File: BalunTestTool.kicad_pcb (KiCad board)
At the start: 2 copper layers, 37.2 x 37.1 mm, 17 parts

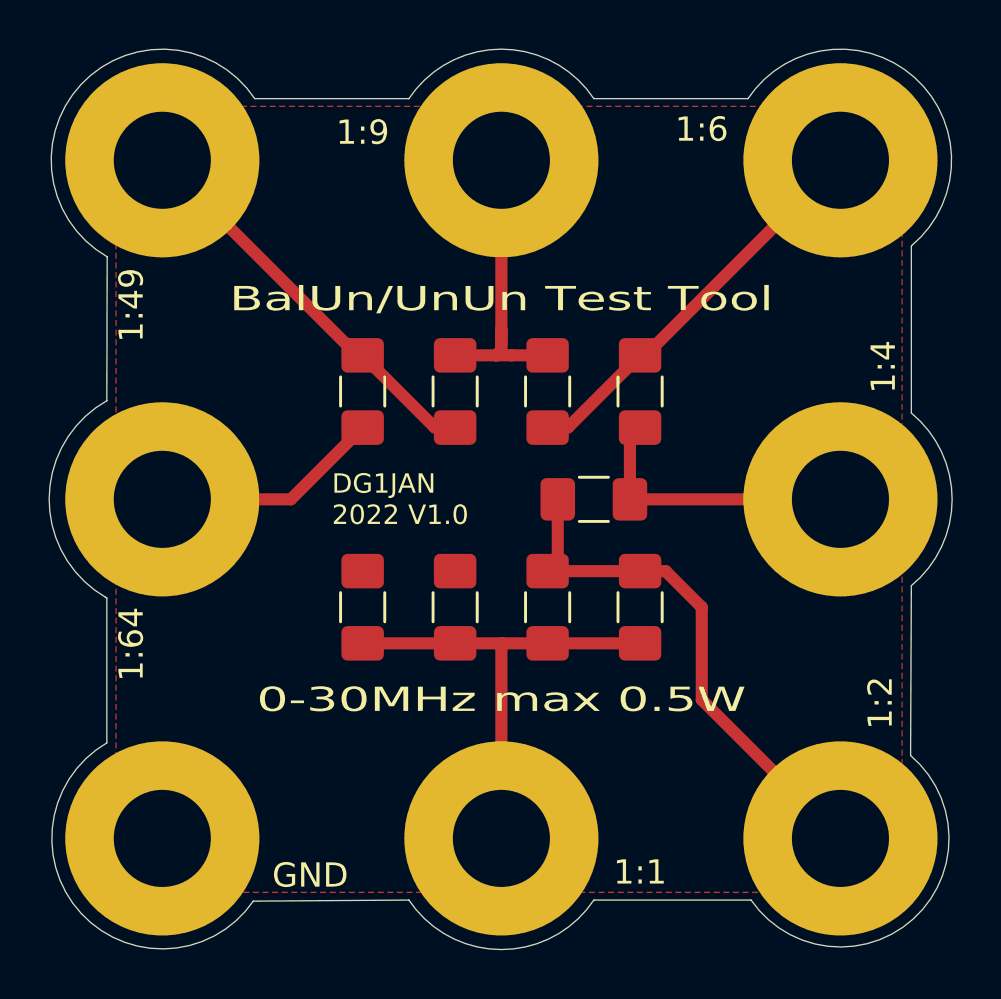
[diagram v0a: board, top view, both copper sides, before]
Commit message: update new version with THT resistors
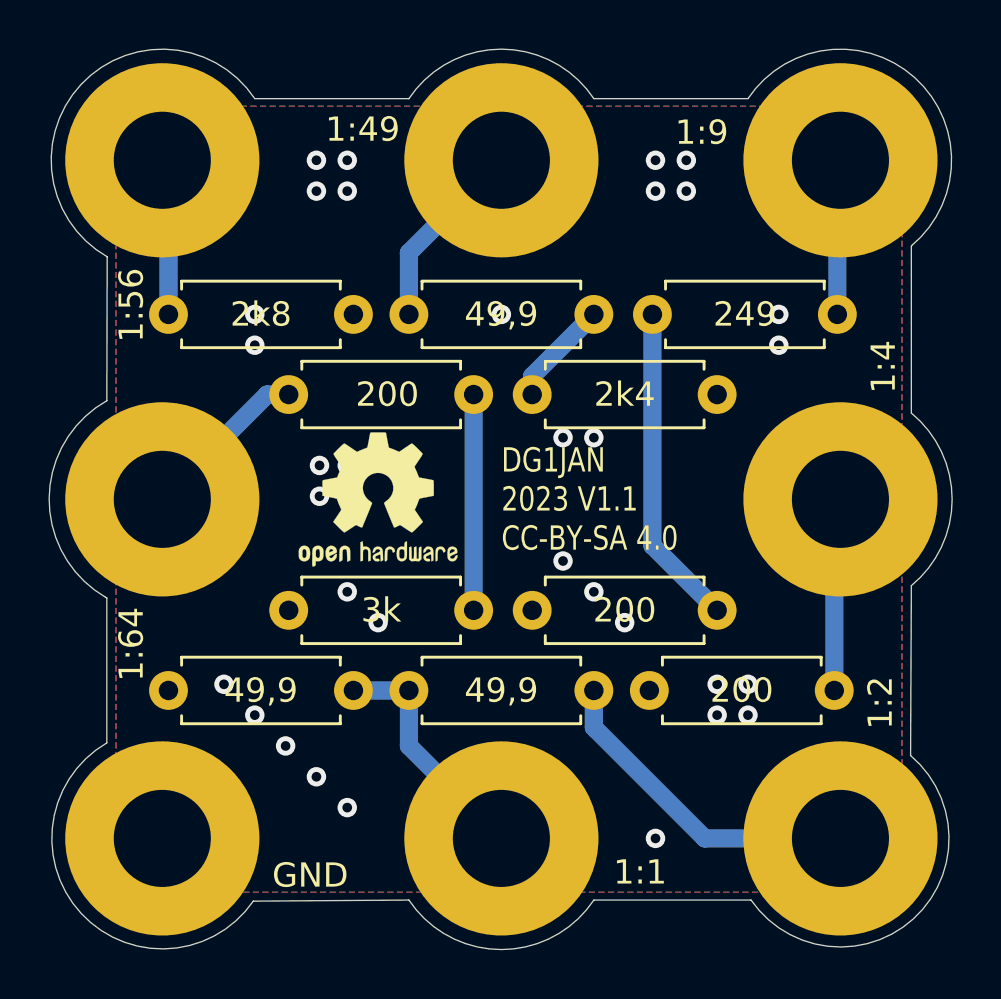
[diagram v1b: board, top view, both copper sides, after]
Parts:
- removed the R4 at (83.2, 98.4)
- added R5: 249, Resistor_THT:R_Axial_DIN0207_L6.3mm_D2.5mm_P7.62mm_Horizontal, F.Cu at (91.3, 95.2)
- added R6: 2k4, Resistor_THT:R_Axial_DIN0207_L6.3mm_D2.5mm_P7.62mm_Horizontal, F.Cu at (78.7, 98.6)
- added REF**: OSHW-Logo2_7.3x6mm_SilkScreen, Symbol:OSHW-Logo2_7.3x6mm_SilkScreen, F.Cu at (72.4, 102.9)
- 1:49: renamed from 1:6; value 1:6 -> 1:49
- 1:56: renamed from 1:49; value 1:49 -> 1:56
- R1, R2: value 100 -> 49,9; footprint Resistor_SMD:R_1206_3216Metric_Pad1.42x1.75mm_HandSolder -> Resistor_THT:R_Axial_DIN0207_L6.3mm_D2.5mm_P7.62mm_Horizontal
- R10, R3: value 100 -> 200; footprint Resistor_SMD:R_1206_3216Metric_Pad1.42x1.75mm_HandSolder -> Resistor_THT:R_Axial_DIN0207_L6.3mm_D2.5mm_P7.62mm_Horizontal
- R4: renamed from R6; value 150 -> 200; footprint Resistor_SMD:R_1206_3216Metric_Pad1.42x1.75mm_HandSolder -> Resistor_THT:R_Axial_DIN0207_L6.3mm_D2.5mm_P7.62mm_Horizontal
- R7: value 2k -> 49,9; footprint Resistor_SMD:R_1206_3216Metric_Pad1.42x1.75mm_HandSolder -> Resistor_THT:R_Axial_DIN0207_L6.3mm_D2.5mm_P7.62mm_Horizontal
- R8: value 750 -> 2k8; footprint Resistor_SMD:R_1206_3216Metric_Pad1.42x1.75mm_HandSolder -> Resistor_THT:R_Axial_DIN0207_L6.3mm_D2.5mm_P7.62mm_Horizontal
- R9: value 100 -> 3k; footprint Resistor_SMD:R_1206_3216Metric_Pad1.42x1.75mm_HandSolder -> Resistor_THT:R_Axial_DIN0207_L6.3mm_D2.5mm_P7.62mm_Horizontal
- moved R10 16.9 mm to (68.7, 98.6), turned to 0 degrees
- moved 1:49 14.0 mm to (77.5, 88.9)
- moved 1:9 14.0 mm to (91.4, 88.9)
- moved R3 12.7 mm to (91.2, 110.7)
- moved R4 11.4 mm to (86.4, 107.4), turned to 180 degrees
- moved R8 8.61 mm to (63.8, 95.2), turned to 0 degrees
- moved R2 3.92 mm to (81.3, 110.7), turned to 180 degrees
- moved R7 3.70 mm to (73.7, 95.2), turned to 0 degrees
- moved R1 3.45 mm to (71.4, 110.7), turned to 180 degrees
- moved R9 0.77 mm to (76.3, 107.4), turned to 180 degrees
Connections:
- 1:49 pad 1: Net-(H5-Pad1) -> Net-(H6-Pad1)
- 1:9 pad 1: Net-(H6-Pad1) -> Net-(H5-Pad1)
- R10 pad 1: Net-(H3-Pad1) -> Net-(H8-Pad1)
- R10 pad 2: Net-(H2-Pad1) -> Net-(R10-Pad2)
- R3 pad 2: Net-(H3-Pad1) -> Net-(H1-Pad1)
- R4 pad 1: Net-(H6-Pad1) -> Net-(R4-Pad1)
- R4 pad 2: Net-(H5-Pad1) -> Net-(H1-Pad1)
- R7 pad 1: Net-(H7-Pad1) -> Net-(H6-Pad1)
- R7 pad 2: Net-(H6-Pad1) -> Net-(R6-Pad1)
- R8 pad 1: Net-(H8-Pad1) -> Net-(H7-Pad1)
- R8 pad 2: Net-(H7-Pad1) -> Net-(H1-Pad1)
- R9 pad 1: Net-(H2-Pad1) -> Net-(R10-Pad2)
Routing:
- net Net-(R4-Pad1): track 0.00 -> 13.3 mm
- net Net-(H7-Pad1): track 17.3 -> 6.46 mm
- net Net-(H5-Pad1): track 16.8 -> 6.40 mm
- net Net-(H2-Pad1): track 19.5 -> 9.96 mm
- net Net-(R10-Pad2): track 0.00 -> 8.89 mm
- net Net-(H3-Pad1): track 22.4 -> 13.6 mm
- net Net-(H6-Pad1): track 12.6 -> 7.93 mm
- net Net-(R6-Pad1): track 0.00 -> 4.35 mm
- net Net-(H4-Pad1): track 11.8 -> 7.98 mm
- net Net-(H8-Pad1): track 9.48 -> 7.00 mm
- net Net-(H1-Pad1): vias 0 -> 34
- added copper zone on B.Cu, net Net-(H1-Pad1)
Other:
- net class Default removed
- board text added: "DG1JAN 2023 V1.1 CC-BY-SA 4.0"
- board text removed: "0-30MHz max 0.5W"
- board text removed: "BalUn/UnUn Test Tool"
- board text removed: "DG1JAN 2022 V1.0"
